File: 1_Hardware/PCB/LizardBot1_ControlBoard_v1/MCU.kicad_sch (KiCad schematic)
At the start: 30 parts, among them J301 2.54mm (F), J302 2.54mm (F), J303 USB_C_Receptacle_USB2.0_16P, Q301 UMH3N, SW301 SW_Push, SW302 SW_Push, SW303 SW_SPST, U301 ESP32-WROOM-32E, U302 USBLC6-2P6, U303 CP2102N-Axx-xQFN24

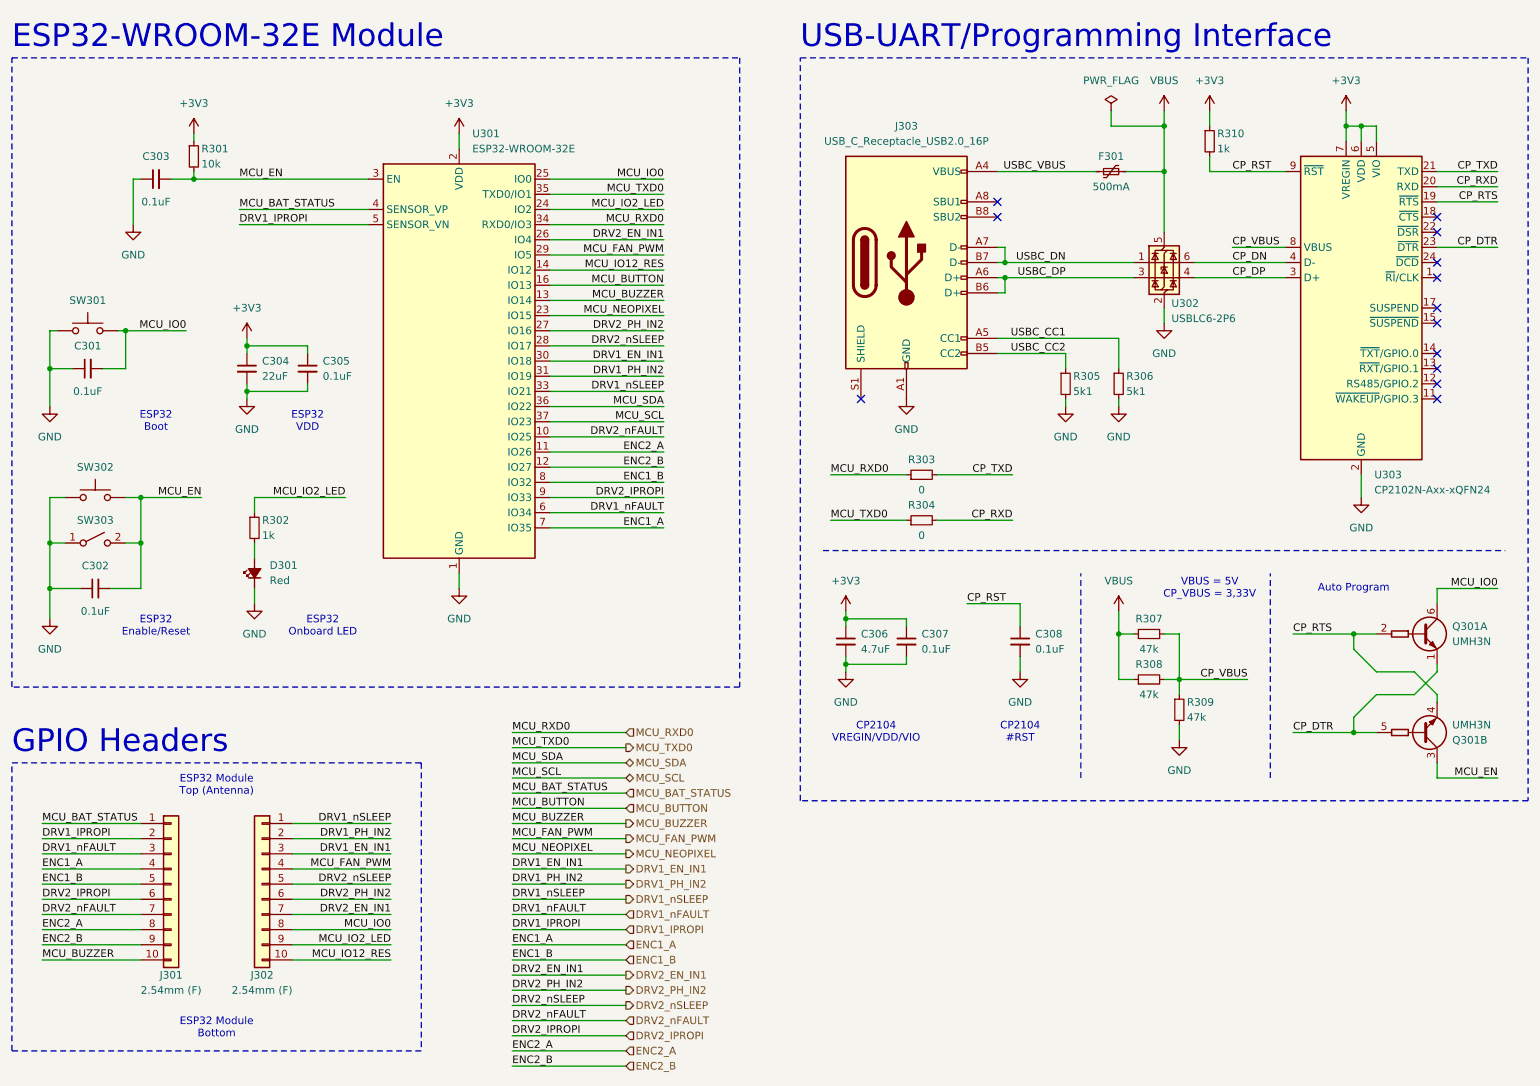
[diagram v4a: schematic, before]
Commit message: Finished PCB routing. Updated ESP32 GPIO layout.
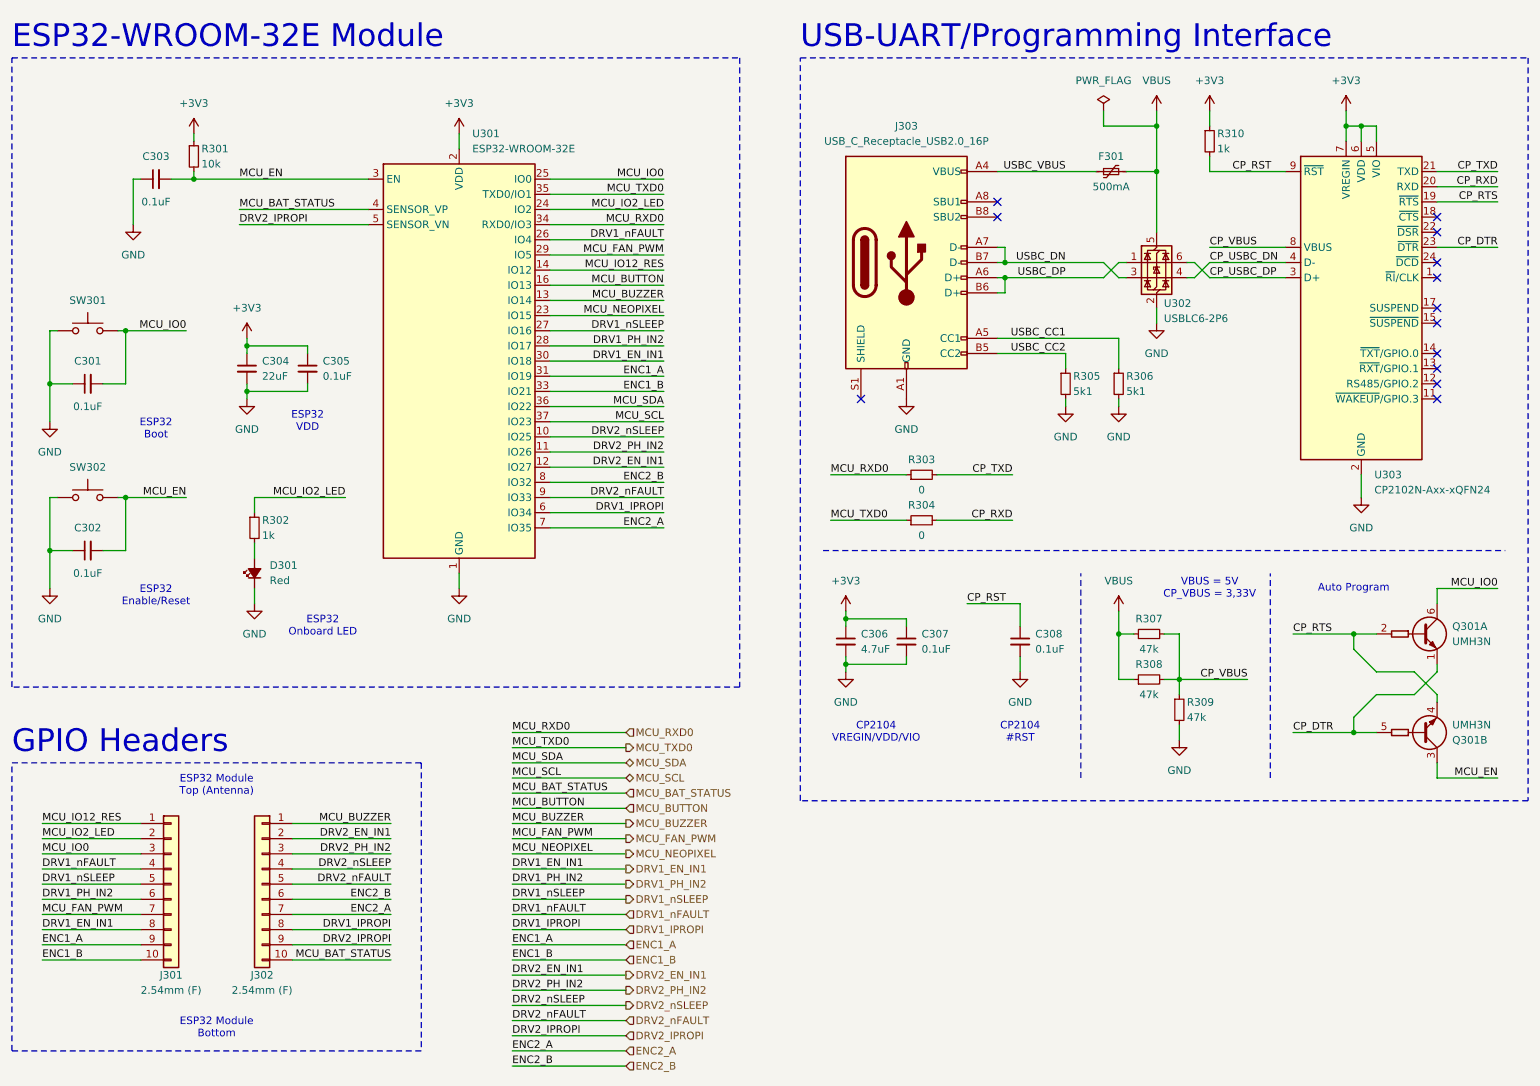
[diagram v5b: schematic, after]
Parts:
- removed SW303: SW_SPST, Button_Switch_THT:SW_Slide_SPDT_Straight_CK_OS102011MS2Q, symbol Switch:SW_SPST
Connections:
- net DRV1_EN_IN1: now also J301.8 (Pin_8); no longer J302.3 (Pin_3)
- net DRV1_IPROPI: now also J302.8 (Pin_8), U301.6 (IO34); no longer J301.2 (Pin_2), U301.5 (SENSOR_VN)
- net DRV1_PH_IN2: now also J301.6 (Pin_6), U301.28 (IO17); no longer J302.2 (Pin_2), U301.31 (IO19)
- net DRV1_nFAULT: now also J301.4 (Pin_4), U301.26 (IO4); no longer J301.3 (Pin_3), U301.6 (IO34)
- net DRV1_nSLEEP: now also J301.5 (Pin_5), U301.27 (IO16); no longer J302.1 (Pin_1), U301.33 (IO21)
- net DRV2_EN_IN1: now also J302.2 (Pin_2), U301.12 (IO27); no longer J302.7 (Pin_7), U301.26 (IO4)
- net DRV2_IPROPI: now also J302.9 (Pin_9), U301.5 (SENSOR_VN); no longer J301.6 (Pin_6), U301.9 (IO33)
- net DRV2_PH_IN2: now also J302.3 (Pin_3), U301.11 (IO26); no longer J302.6 (Pin_6), U301.27 (IO16)
- net DRV2_nFAULT: now also J302.5 (Pin_5), U301.9 (IO33); no longer J301.7 (Pin_7), U301.10 (IO25)
- net DRV2_nSLEEP: now also J302.4 (Pin_4), U301.10 (IO25); no longer J302.5 (Pin_5), U301.28 (IO17)
- net ENC1_A: now also J301.9 (Pin_9), U301.31 (IO19); no longer J301.4 (Pin_4), U301.7 (IO35)
- net ENC1_B: now also J301.10 (Pin_10), U301.33 (IO21); no longer J301.5 (Pin_5), U301.8 (IO32)
- net ENC2_A: now also J302.7 (Pin_7), U301.7 (IO35); no longer J301.8 (Pin_8), U301.11 (IO26)
- net ENC2_B: now also J302.6 (Pin_6), U301.8 (IO32); no longer J301.9 (Pin_9), U301.12 (IO27)
- net MCU_BAT_STATUS: now also J302.10 (Pin_10); no longer J301.1 (Pin_1)
- net MCU_BUZZER: now also J302.1 (Pin_1); no longer J301.10 (Pin_10)
- net MCU_FAN_PWM: now also J301.7 (Pin_7); no longer J302.4 (Pin_4)
- net MCU_IO0: now also J301.3 (Pin_3); no longer J302.8 (Pin_8)
- net MCU_IO12_RES: now also J301.1 (Pin_1); no longer J302.10 (Pin_10)
- net MCU_IO2_LED: now also J301.2 (Pin_2); no longer J302.9 (Pin_9)
- net USBC_DN: now also U302.3 (I/O2); no longer U302.1 (I/O1)
- net USBC_DP: now also U302.1 (I/O1); no longer U302.3 (I/O2)
- net CP_DN renamed CP_USBC_DN
- net CP_USBC_DN: now also U302.4 (I/O2); no longer U302.6 (I/O1)
- net CP_DP renamed CP_USBC_DP
- net CP_USBC_DP: now also U302.6 (I/O1); no longer U302.4 (I/O2)
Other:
- moved on the sheet: C301, C302, SW302, U302
